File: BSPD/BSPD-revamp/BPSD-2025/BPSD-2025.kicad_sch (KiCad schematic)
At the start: 10 parts, among them U1 NE555DR, U101 641964-1, U102 641964-1

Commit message: Worked on BSPD
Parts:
- removed RV1: 10k, symbol Device:R_Potentiometer_US
- removed U101, U102: 641964-1, 641964-1:641964-1_TYC, symbol 641964-1:641964-1
- added C1, C2: 10uF, symbol Device:C
- added J1: Conn(APPS_ABC), symbol Connector:Conn_01x03_Pin
- added J2: Conn(APPS_DEF), symbol Connector:Conn_01x03_Pin
- added J3: Conn(12V,GND), symbol Connector:Conn_01x02_Pin
- added J4: Conn(BSE), symbol Connector:Conn_01x03_Pin
- added R1, R3: 10k, symbol Device:R_US
- added R2, R4: 6.8k, symbol Device:R_US
- added U104: R-78E5.0-0.5, R_78E5_0_0_5:R-78E-0.5_RCP, symbol R_78E5_0_0_5:R-78E5.0-0.5
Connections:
- net +5V: now also C2.1, J4.1 (Pin_1), U104.3 (+VOUT)
- net GND: now also C1.2, C2.2, J1.3 (Pin_3), J2.3 (Pin_3), J3.2 (Pin_2), J4.3 (Pin_3), R2.2, R4.2, U104.2 (GND)
- net THRES_APPS renamed THRES_APPS_B
- net THRES_APPS 1 renamed THRES_APPS_E
- new net +12V: C1.1, J1.1 (Pin_1), J2.1 (Pin_1), J3.1 (Pin_1), U104.1 (+VIN)
- new net APPS_B_12V: J1.2 (Pin_2), R1.1
- new net APPS_B_5V: R1.2, R2.1
- new net APPS_E_12V: J2.2 (Pin_2), R3.1
- new net APPS_E_5V: R3.2, R4.1
- new net BSE_5V: J4.2 (Pin_2)
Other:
- note added: "APPS internals"
- note added: "BSE"
- note added: "VINH PUT THE BSE INPUTS HERE"
- moved on the sheet: C105, C108, R103, RV2, RV3, RV4, U1

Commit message: APPS DCDC converter switch-up
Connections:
- net +12V: no longer J2.1 (Pin_1)
- net +5V: now also J2.1 (Pin_1)
- net APPS_E_12V: no longer J2.2 (Pin_2)
- net APPS_E_5V: now also J2.2 (Pin_2)
- net GND: no longer C1.2, J1.3 (Pin_3), J2.3 (Pin_3), J3.2 (Pin_2)
- new net GNDPWR: C1.2, J1.3 (Pin_3), J3.2 (Pin_2)
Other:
- note removed: "VINH PUT THE BSE INPUTS HERE"
- moved on the sheet: C1, C105, C108, C2, J1, J2, J3, J4, R1, R103, R2, R3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

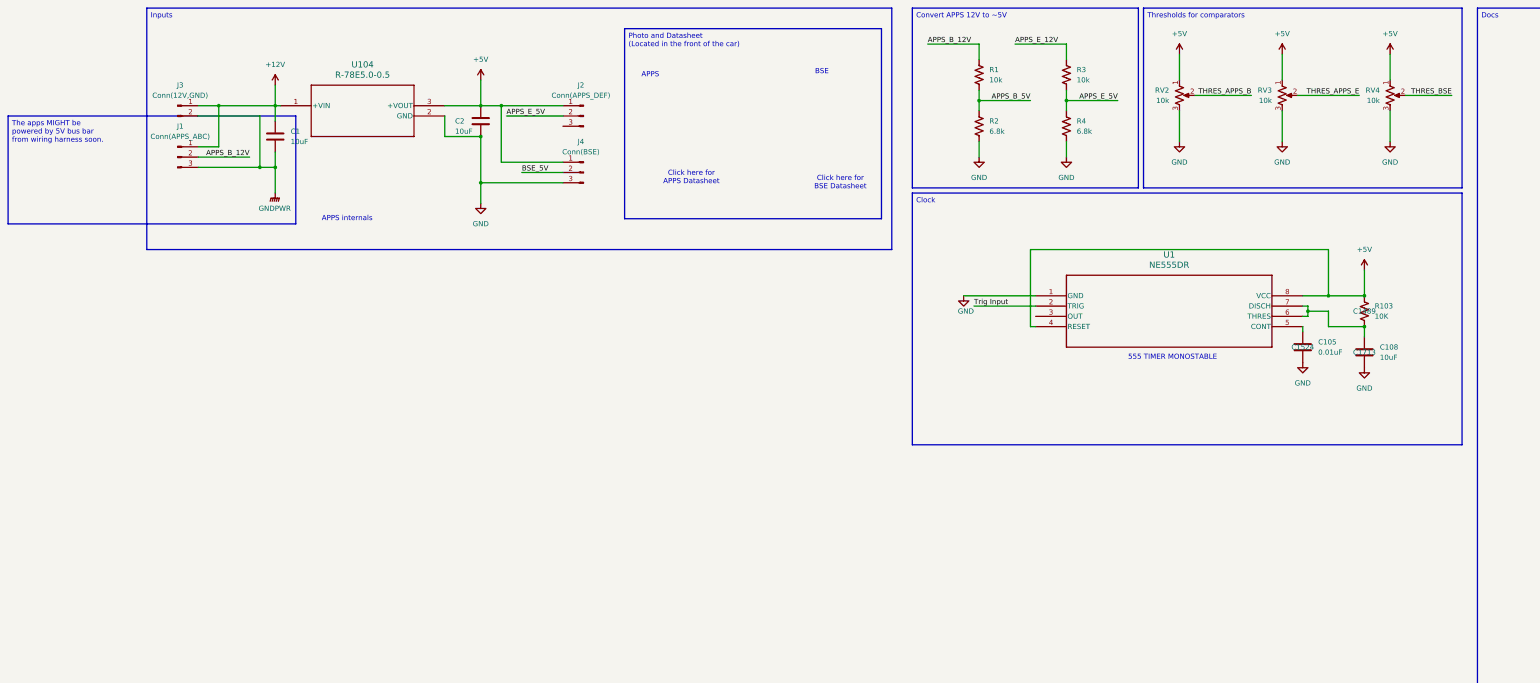
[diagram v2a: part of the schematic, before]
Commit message: BSPD Added comparator
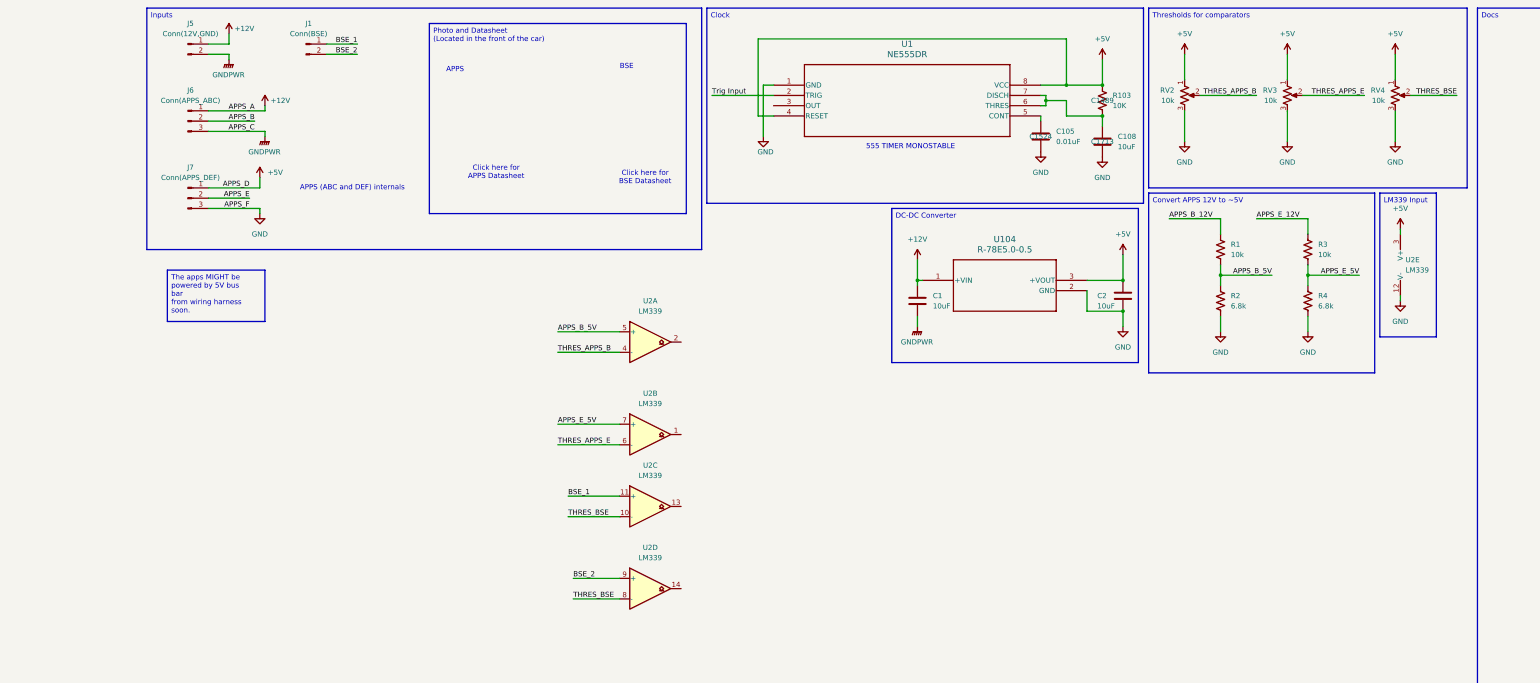
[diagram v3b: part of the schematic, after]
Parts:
- removed J1: Conn(APPS_ABC), symbol Connector:Conn_01x03_Pin
- removed J2: Conn(APPS_DEF), symbol Connector:Conn_01x03_Pin
- removed J3: Conn(12V,GND), symbol Connector:Conn_01x02_Pin
- removed J4: Conn(BSE), symbol Connector:Conn_01x03_Pin
- added J1: Conn(BSE), symbol Connector:Conn_01x02_Pin
- added J5: Conn(12V,GND), symbol Connector:Conn_01x02_Pin
- added J6: Conn(APPS_ABC), symbol Connector:Conn_01x03_Pin
- added J7: Conn(APPS_DEF), symbol Connector:Conn_01x03_Pin
- added U2: LM339, symbol Comparator:LM339
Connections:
- net +12V: now also J5.1 (Pin_1), J6.1 (Pin_1)
- net +5V: now also J7.1 (Pin_1), U2.3 (V+)
- net APPS_B_5V: now also U2.5 (+)
- net APPS_E_5V: now also U2.7 (+)
- net GND: now also J7.3 (Pin_3), U2.12 (V-)
- net GNDPWR: now also J5.2 (Pin_2), J6.3 (Pin_3)
- net THRES_APPS_B: now also U2.4 (-)
- net THRES_APPS_E: now also U2.6 (-)
- net THRES_BSE: now also U2.10 (-), U2.8 (-)
- new net APPS_B: J6.2 (Pin_2)
- new net APPS_E: J7.2 (Pin_2)
- new net BSE_1: J1.1 (Pin_1), U2.11 (+)
- new net BSE_2: J1.2 (Pin_2), U2.9 (+)
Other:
- note added: "APPS (ABC and DEF) internals"
- note removed: "APPS internals"
- moved on the sheet: C1, C105, C108, C2, R1, R103, R2, R3, R4, RV2, RV3, RV4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

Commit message: Worked on BSPD
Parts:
- added C3: 100uF, symbol Device:C
- added R10: 15k, symbol Device:R_US
- added R5, R6, R7, R8: 100k, symbol Device:R_US
- added R9: 10k, symbol Device:R_US
- added RV5: 10k, symbol Device:R_Potentiometer_US
- added U3: 74AUC2G32, symbol 74xGxx:74AUC2G32
- added U4: 74AUC2G08, symbol 74xGxx:74AUC2G08
- added U5: LM339, symbol Comparator:LM339
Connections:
- net +5V: now also R10.1, R5.1, R6.1, R7.1, R8.1, RV5.1
- net GND: now also C3.2, RV5.3
- net at U2.14: now also R7.2, U3.6
- net at U2.2: now also R8.2, U3.1
- net at U2.13: now also R6.2, U3.5
- net at U2.1: now also R5.2, U3.2
- new net: U3.7, U4.1
- new net: C3.1, R9.2, U5.11 (+)
- new net: U3.3, U4.2
- new net: R9.1, U4.7
- new net BSPD_OUT: R10.2, U5.13
- new net THRES_CHARGE: RV5.2, U5.10 (-)
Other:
- note added: "7408 Input"
- note added: "7432 Input"
- note added: "all logic should be CMOS"
- note added: "τ = 1s"
- moved on the sheet: C105, C108, R103, U1, U2A, U2B, U2C, U2D, U2E

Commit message: Put BPSD foorprints
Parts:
- R10, R5, R6, R7, R8, R9: footprint (none) -> Resistor_SMD:R_0603_1608Metric

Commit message: Hopefully BSPD is Final
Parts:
- removed C105: 0.01uF, Capacitor_SMD:C_0402_1005Metric, symbol Device:C
- removed C108: 10uF, Capacitor_SMD:C_0805_2012Metric, symbol Device:C
- removed J1: Conn(BSE), symbol Connector:Conn_01x02_Pin
- removed J6: Conn(APPS_ABC), symbol Connector:Conn_01x03_Pin
- removed J7: Conn(APPS_DEF), symbol Connector:Conn_01x03_Pin
- removed R1, R3: 10k, symbol Device:R_US
- removed R103: 10K, Resistor_SMD:R_1206_3216Metric, symbol Device:R_US
- removed R2, R4: 6.8k, symbol Device:R_US
- removed R5: 100k, Resistor_SMD:R_0603_1608Metric, symbol Device:R_US
- removed RV3: 10k, symbol Device:R_Potentiometer_US
- removed U1: NE555DR, D8, symbol NE555DR:NE555DR
- removed unit 2 of U2
- removed unit 1 of U3
- added J1: Conn(BSE_1), symbol Connector:Conn_01x03_Pin
- added J2: Conn(BSE_2), symbol Connector:Conn_01x03_Pin
- added J6: Conn(Hall Effect), symbol Connector:Conn_01x02_Pin
- J5: value Conn(12V,GND) -> Conn(12V)
- R9: value 10k -> 1k
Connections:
- net +5V: now also J1.1 (Pin_1), J2.1 (Pin_1)
- net BSE_1: now also J1.2 (Pin_2)
- net BSE_2: now also J2.2 (Pin_2)
- net GND: now also J1.3 (Pin_3), J2.3 (Pin_3), J6.2 (Pin_2)
- net THRES_CHARGE: no longer RV5.2
- net at R8.2, U2.2: now also U4.1
- net APPS_B_5V renamed ACCUM_V
- net ACCUM_V: now also J6.1 (Pin_1)
- net THRES_APPS_B renamed THRESH_ACCUM
- net THRES_BSE renamed THRESH_BSE
- new net THRESH_CHARGE: RV5.2
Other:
- note added: "BMS Voltage (0-5V)"
- note added: "BSE Voltage (0-5V)"
- note added: "Current Sensor"
- note added: "τ = 0.1s"
- note removed: "555 TIMER MONOSTABLE"
- note removed: "APPS"
- note removed: "APPS (ABC and DEF) internals"
- note removed: "all logic should be CMOS"
- note removed: "τ = 1s"
- moved on the sheet: C1, C2, C3, J5, R10, R6, R7, R8, R9, RV2, RV5, U104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

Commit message: BSPD Stuff
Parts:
- added C4, C5, C6, C7, C8, C9: 0.1uF, symbol Device:C
- added TP10: TP_GND, symbol Connector:TestPoint
- added TP4: TP_BSE_1, symbol Connector:TestPoint
- added TP5: TB_BSE_2, symbol Connector:TestPoint
- added TP6: TP_ACCUM_V, symbol Connector:TestPoint
- added TP7: TP_CHARGE, symbol Connector:TestPoint
- added TP8: TP_ACCUM, symbol Connector:TestPoint
- added TP9: TP_BSE, symbol Connector:TestPoint
- R9: value 1k -> 2.2k
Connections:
- net +5V: now also C5.1, C6.1
- net ACCUM_V: now also C4.1, C7.1, TP6.1
- net BSE_1: now also C8.1, TP4.1
- net BSE_2: now also C9.1, TP5.1
- net GND: now also C4.2, C5.2, C6.2, C7.2, C8.2, C9.2, TP10.1
- net THRESH_ACCUM: now also TP8.1
- net THRESH_BSE: now also TP9.1
- net THRESH_CHARGE: now also TP7.1
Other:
- moved on the sheet: C3, J1, R10, R6, R7, R8, R9, RV2, RV4, U2A, U2C, U2D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

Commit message: Description of work done in commit
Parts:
- removed C1: 10uF, symbol Device:C
- removed C3: 100uF, symbol Device:C
- removed C5, C6, C7, C8, C9: 0.1uF, symbol Device:C
- removed J1: Conn(BSE_1), symbol Connector:Conn_01x03_Pin
- removed J2: Conn(BSE_2), symbol Connector:Conn_01x03_Pin
- removed J5: Conn(12V), symbol Connector:Conn_01x02_Pin
- removed J6: Conn(Hall Effect), symbol Connector:Conn_01x02_Pin
- removed R10: 15k, Resistor_SMD:R_0603_1608Metric, symbol Device:R_US
- removed R6, R7, R8: 100k, Resistor_SMD:R_0603_1608Metric, symbol Device:R_US
- removed R9: 2.2k, Resistor_SMD:R_0603_1608Metric, symbol Device:R_US
- removed RV2, RV4, RV5: 10k, symbol Device:R_Potentiometer_US
- removed TP4: TP_BSE_1, symbol Connector:TestPoint
- removed TP5: TB_BSE_2, symbol Connector:TestPoint
- removed TP6: TP_ACCUM_V, symbol Connector:TestPoint
- removed TP7: TP_CHARGE, symbol Connector:TestPoint
- removed U104: R-78E5.0-0.5, R_78E5_0_0_5:R-78E-0.5_RCP, symbol R_78E5_0_0_5:R-78E5.0-0.5
- removed U2, U5: LM339, symbol Comparator:LM339
- removed U3: 74AUC2G32, symbol 74xGxx:74AUC2G32
- removed U4: 74AUC2G08, symbol 74xGxx:74AUC2G08
- added C10, C11: 100uF, Capacitor_SMD:C_1206_3216Metric, symbol Device:C
- added C13, C14, C15, C16, C17, C18, C19, C20, C21, C22, C23, C24, C25, C26: 0.1uF, Capacitor_SMD:C_1206_3216Metric, symbol Device:C
- added J1, J2: SAMMY-3PIN, BSPD:SAMMY-3PIN, symbol BSPD:SAMMY-3PIN
- added J3, J5: SAMMY-2PIN, BSPD:SAMMY-2PIN, symbol BSPD:SAMMY-2PIN
- added J4: SAMMY-5PIN, BSPD:SAMMY-5PIN, symbol BSPD:SAMMY-5PIN
- added Q1, Q2: NMOS, Package_TO_SOT_SMD:SOT-23, symbol Simulation_SPICE:NMOS
- added R11, R12, R13, R14, R15, R16, R17, R21, R24: 100k, Resistor_SMD:R_1210_3225Metric, symbol Device:R_US
- added R18: 2.2k, Resistor_SMD:R_1210_3225Metric, symbol Device:R_US
- added R19, R22: 10k, Resistor_SMD:R_1210_3225Metric, symbol Device:R_US
- added R20, R23: 1k, Resistor_SMD:R_1210_3225Metric, symbol Device:R_US
- added RV6, RV7: 10k, Potentiometer_THT:Potentiometer_Bourns_3296W_Vertical, symbol Device:R_Potentiometer_US
- added U10, U12, U4, U5, U6, U9: LM397, Package_TO_SOT_SMD:SOT-23-5, symbol Comparator:LM397
- added U11, U7: SN74AHC1G08DBVR, Package_TO_SOT_SMD:SOT-23-5, symbol 74xGxx:74AHC1G08
- added U17, U18: SN74AHC1G32DBVR, Package_TO_SOT_SMD:SOT-23-5, symbol 74xGxx:74AHC1G32
- added U3: LM1117DT-5.0, Package_TO_SOT_SMD:TO-252-3_TabPin2, symbol Regulator_Linear:LM1117DT-5.0
- added U8: SN74AHC1G00DBVR, Package_TO_SOT_SMD:SOT-23-5, symbol 74xGxx:74AHC1G00
- C2: footprint (none) -> Capacitor_SMD:C_1206_3216Metric; JLC# (none) -> C1849
- C4: value 0.1uF -> 10uF; footprint (none) -> Capacitor_SMD:C_1206_3216Metric; JLC# (none) -> C1849
- TP10, TP8, TP9: footprint (none) -> TestPoint:TestPoint_Pad_D1.5mm
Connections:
- net +12V: now also C4.1, J3.2, R19.2, U3.3 (VI)
- net +5V: now also C13.1, C14.1, C15.2, C16.2, C17.2, C18.2, C19.2, C20.2, C21.2, C22.2, C23.2, C24.2, C25.2, C26.1, J1.3, J2.3, J4.5, R11.2, R12.2, R13.2, R15.2, R21.2, R22.2, R24.2, RV6.1, RV7.1, U10.5 (V+), U11.5 (VCC), U12.5 (V+), U17.5 (VCC), U18.5 (VCC), U3.2 (VO), U4.5 (V+), U5.5 (V+), U6.5 (V+), U7.5 (VCC), U8.5 (VCC), U9.5 (V+)
- net ACCUM_V: now also J4.3, R14.2, U4.3 (+), U9.3 (+); no longer C4.1
- net BSE_1: now also J1.1, R17.2, U10.3 (+), U5.3 (+)
- net BSE_2: now also J2.1, R16.2, U12.3 (+), U6.3 (+)
- net BSPD_OUT: now also J5.1, Q2.1 (D)
- net GND: now also C10.2, C11.2, C13.2, C14.2, C15.1, C16.1, C17.1, C18.1, C19.1, C20.1, C21.1, C22.1, C23.1, C24.1, C25.1, C26.2, J1.2, J2.2, J3.1, J4.4, Q1.3 (S), Q2.3 (S), R14.1, R16.1, R17.1, R23.1, RV6.3, RV7.3, U10.2 (V-), U11.3 (GND), U12.2 (V-), U17.3 (GND), U18.3 (GND), U3.1 (GND), U4.2 (V-), U5.2 (V-), U6.2 (V-), U7.3 (GND), U8.3 (GND), U9.2 (V-)
- net THRESH_ACCUM: now also RV6.2, U4.1 (-)
- net THRESH_BSE: now also RV7.2, U5.1 (-), U6.1 (-)
- new net: C10.1, R20.2, U17.1
- new net: C11.1, R18.2, U17.2
- new net: Q1.2 (G), U17.4
- new net: R24.1, U12.4, U7.2
- new net: R21.1, U10.4, U7.1
- new net: U7.4, U8.2
- new net: R15.1, U8.1, U9.4
- new net: R13.1, U18.2, U6.4
- new net: Q1.1 (D), Q2.2 (G), R19.1
- new net: R11.1, U11.1, U4.4
- new net: R12.1, U18.1, U5.4
- new net: U11.2, U18.4
- new net 0.455V: R22.1, R23.2, U10.1 (-), U12.1 (-), U9.1 (-)
- new net BRAKE+CURRENT_HOLD: R18.1, U11.4
- new net DISCONNECT_HOLD: R20.1, U8.4
- no-connect marks 0 -> 3
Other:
- note added: "220 ohm resistor in series with 12V from FL here"
- note added: "5V"
- note added: "BSE Voltage (0.5-4.5V)"
- note added: "GND"
- note added: "NC"
- note added: "OUT"
- note added: "https://jlcpcb.com/partdetail/BOURNS-3361P_1103GLF/C840679"
- note added: "τ = 0.22s"
- note removed: "7408 Input"
- note removed: "7432 Input"
- note removed: "BMS Voltage (0-5V)"
- note removed: "BSE Voltage (0-5V)"
